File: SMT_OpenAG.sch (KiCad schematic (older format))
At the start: 1 part

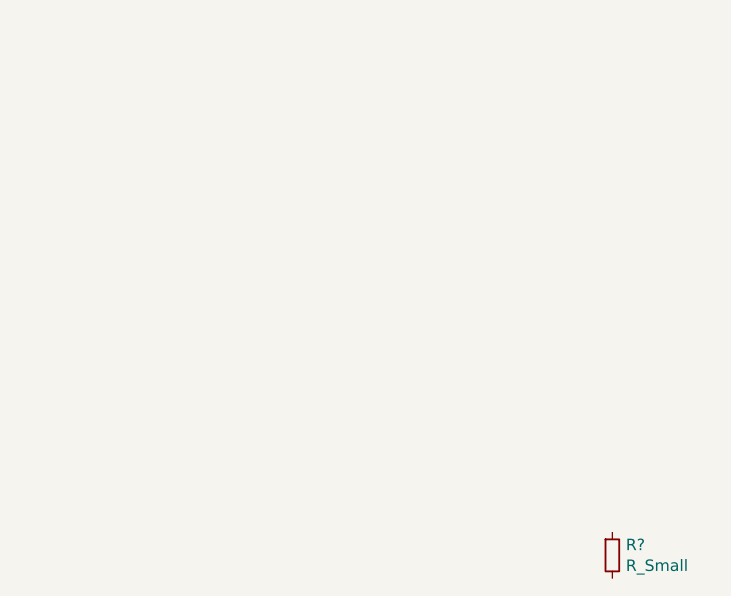
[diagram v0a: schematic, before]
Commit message: added PWM
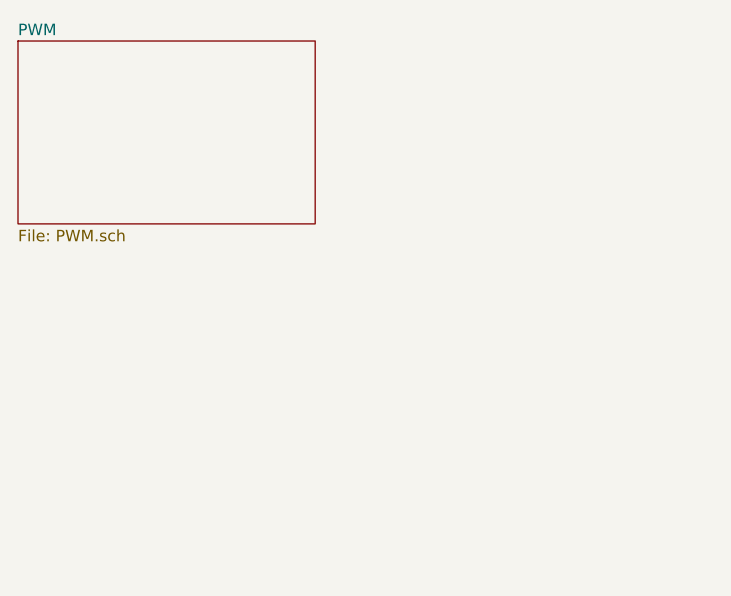
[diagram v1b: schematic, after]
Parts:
- removed R?: R_Small, symbol Device:R_Small
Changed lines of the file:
@@
 $Descr A4 11693 8268
 encoding utf-8
-Sheet 1 1
-Title ""
-Date ""
-Rev ""
+Sheet 1 2
+Title "SMT_OpenAG"
+Date "2020-12-20"
+Rev ".01"
 Comp ""
 Comment1 ""
@@
 Comment4 ""
 $EndDescr
-$Comp
-L Device:R_Small R?
-U 1 1 5FDFEC75
-P 5000 3100
-F 0 "R?" H 5059 3146 50  0000 L CNN
-F 1 "R_Small" H 5059 3055 50  0000 L CNN
-F 2 "" H 5000 3100 50  0001 C CNN
-F 3 "~" H 5000 3100 50  0001 C CNN
-	1    5000 3100
-	1    0    0    -1
-$EndComp
+$Sheet
+S 2400 850  1300 800
+U 5FDFE3AA
+F0 "PWM" 50
+F1 "PWM.sch" 50
+$EndSheet
 $EndSCHEMATC
